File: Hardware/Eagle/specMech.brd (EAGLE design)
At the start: 142.2 x 121.9 mm, 86 parts, among them J1 PINHD-1X8-MOLEX-SHROUD, J2 JST-2-PIN-2B-PH-K-S(LF)(SN), J3 PINHD-1X8-MOLEX-SHROUD, J4 PINHD-1X8-MOLEX-SHROUD, J6 Molex 0022232081, J7 Lantronix XPORT, J8 Molex 0022232081, U1 MCP23008-E/SO, U10 ADS1115, U11 MCP23008-E/SO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

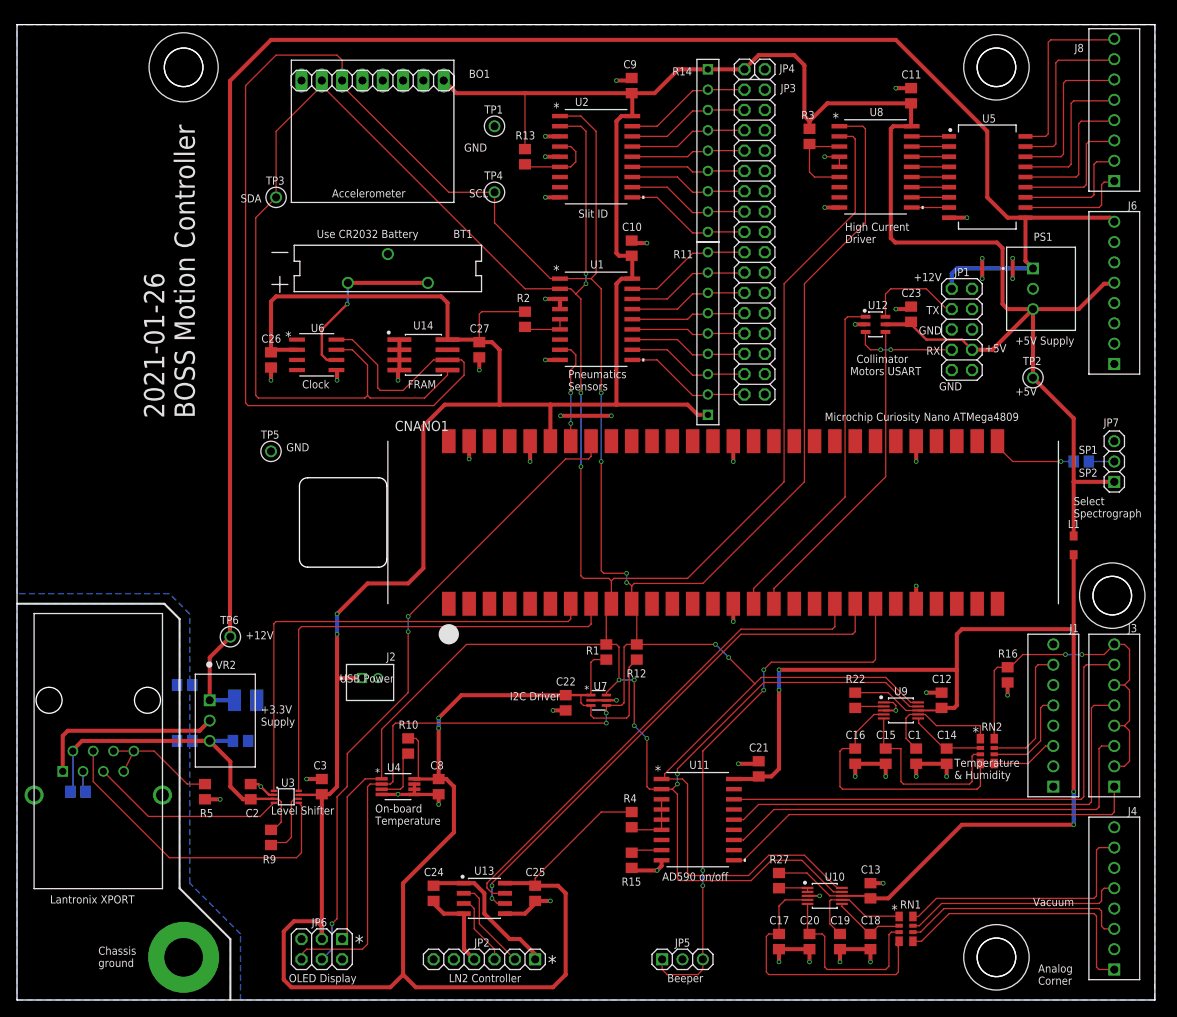
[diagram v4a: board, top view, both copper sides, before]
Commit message: Molex 1x2 header replaces JST header
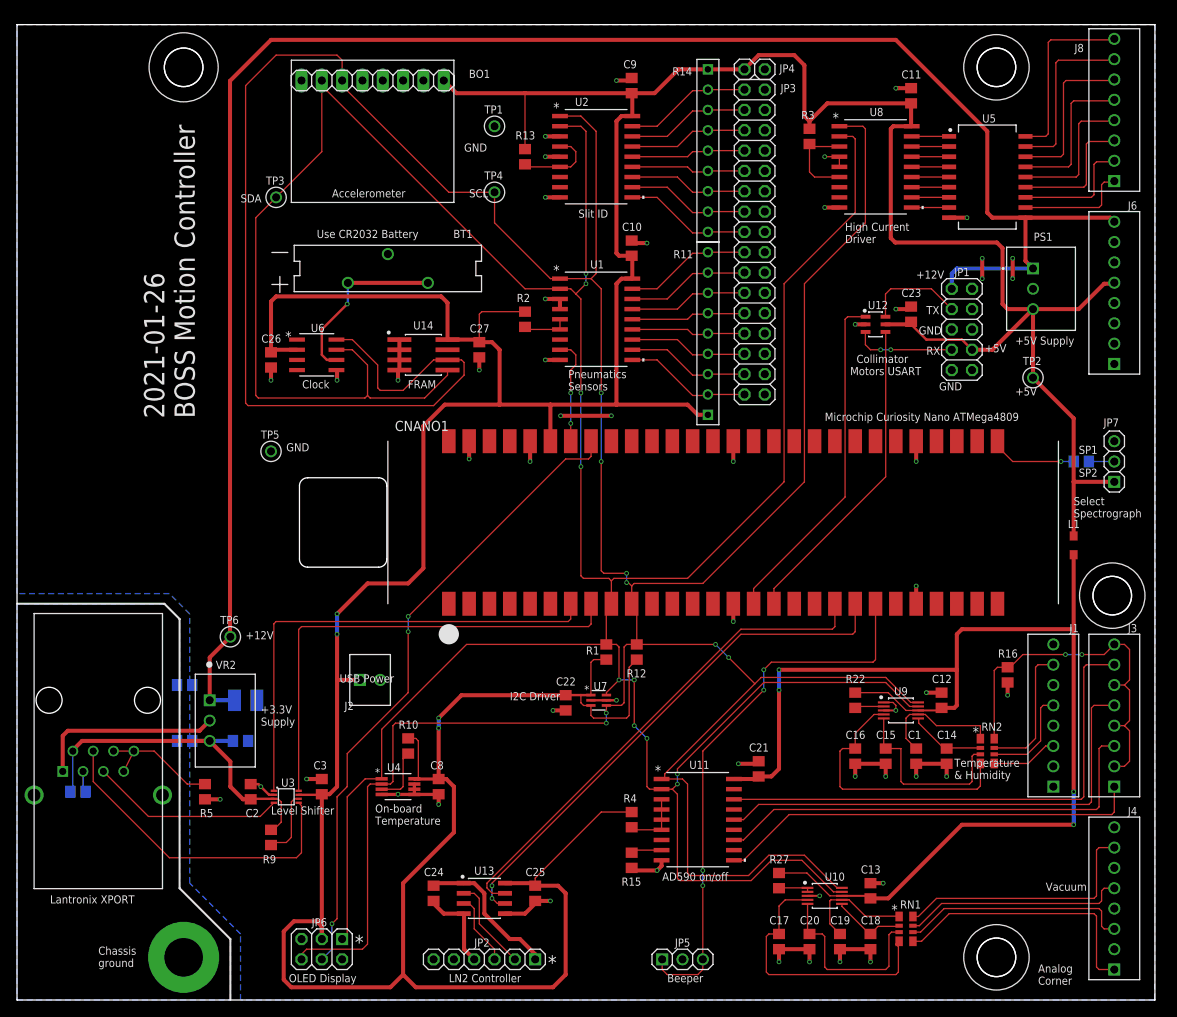
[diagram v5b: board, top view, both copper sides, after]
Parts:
- J2: value JST-2-PIN-2B-PH-K-S(LF)(SN) -> MOLEX-22112022; device AUmlib:JST_B2B-PH-K-S(LF)(SN) -> AUmlib:1X02-MOLEX-22112022
- moved J2 0.32 mm to (44.1, 40.0), turned to 0 degrees
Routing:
- net +12V: track 227.6 -> 228.7 mm
- net SDA: track 430.4 -> 431.0 mm
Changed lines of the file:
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@@
 <wire x1="142.24" y1="121.92" x2="0" y2="121.92" width="0" layer="20"/>
 <text x="40.3225" y="39.6875" size="1.016" layer="25" font="vector">USB Power</text>
-<text x="112.0775" y="89.8525" size="1.016" layer="25" font="vector">+12V</text>
+<text x="112.395" y="90.17" size="1.016" layer="25" font="vector">+12V</text>
 <text x="120.9675" y="80.9625" size="1.016" layer="25" font="vector">+5V</text>
 <text x="115.2525" y="76.2" size="1.016" layer="25" font="vector">GND</text>
@@
 <text x="31.75" y="23.1775" size="1.016" layer="25" font="vector">Level Shifter</text>
 <text x="4.1275" y="12.065" size="1.016" layer="25" font="vector">Lantronix XPORT</text>
-<text x="127" y="11.7475" size="1.016" layer="25" font="vector">Vacuum</text>
+<text x="128.5875" y="13.6525" size="1.016" layer="25" font="vector">Vacuum</text>
 <text x="117.1575" y="27.6225" size="1.016" layer="25" font="vector">Temperature
 &amp; Humidity</text>
@@
 <attribute name="NAME" x="117.1575" y="90.4875" size="1.016" layer="25" font="vector"/>
 <attribute name="POPULARITY" value="35" x="127" y="83.82" size="1.778" layer="27" rot="R270" display="off"/>
-<attribute name="VALUE" x="113.665" y="90.17" size="1.016" layer="27" font="vector" rot="R270"/>
 </element>
 <element name="U12" library="AUmlib" library_urn="urn:adsk.eagle:library:9166017" package="SOP95P275X110-6" package3d_urn="urn:adsk.eagle:package:9152015/2" value="74HC2G17TSSOP-6" x="107.315" y="84.455" smashed="yes">
@@
 <element name="JP2" library="AUmlib" library_urn="urn:adsk.eagle:library:9166017" package="1X06" package3d_urn="urn:adsk.eagle:package:24493396/1" value="1x6 pinhdr" x="58.42" y="5.08" smashed="yes" rot="R180">
 <attribute name="NAME" x="57.15" y="6.6675" size="1.016" layer="25" font="vector"/>
-<attribute name="VALUE" x="66.04" y="8.255" size="1.27" layer="27" rot="R180"/>
 </element>
 <element name="C24" library="AUmlib" library_urn="urn:adsk.eagle:library:9166017" package="C0805" package3d_urn="urn:adsk.eagle:package:4021265/3" value="0.1uF" x="52.07" y="13.335" smashed="yes" rot="R270">
@@
 </element>
 <element name="J7" library="AUmlib" library_urn="urn:adsk.eagle:library:9166017" package="XPORT-2" package3d_urn="urn:adsk.eagle:package:18328251/5" value="Lantronix XPORT" x="10.16" y="31.115" smashed="yes" rot="R270"/>
-<element name="J2" library="AUmlib" library_urn="urn:adsk.eagle:library:9166017" package="JST_B2B-PH-K-S(LF)(SN)" package3d_urn="urn:adsk.eagle:package:24616272/2" value="JST-2-PIN-2B-PH-K-S(LF)(SN)" x="44.1325" y="39.6875" smashed="yes" rot="R180">
-<attribute name="DESCRIPTION" value=" Connector Header Through Hole 2 position 0.079 (2.00mm) " x="44.1325" y="39.6875" size="1.778" layer="27" rot="R180" display="off"/>
-<attribute name="DIGI-KEY_PART_NUMBER" value="455-1704-ND" x="44.1325" y="39.6875" size="1.778" layer="27" rot="R180" display="off"/>
-<attribute name="MF" value="JST Sales" x="44.1325" y="39.6875" size="1.778" layer="27" rot="R180" display="off"/>
-<attribute name="MP" value="B2B-PH-K-S(LF)(SN)" x="44.1325" y="39.6875" size="1.778" layer="27" rot="R180" display="off"/>
-<attribute name="NAME" x="47.33731875" y="43.43358125" size="1.016" layer="25" font="vector" rot="R180"/>
-<attribute name="PACKAGE" value="None" x="44.1325" y="39.6875" size="1.778" layer="27" rot="R180" display="off"/>
-<attribute name="PURCHASE-URL" value="https://pricing.snapeda.com/search/part/B2B-PH-K-S(LF)(SN)/?ref=eda" x="44.1325" y="39.6875" size="1.778" layer="27" rot="R180" display="off"/>
+<element name="J2" library="AUmlib" library_urn="urn:adsk.eagle:library:9166017" package="1X02-MOLEX-22112022" package3d_urn="urn:adsk.eagle:package:24727026/5" value="MOLEX-22112022" x="44.1325" y="40.005" smashed="yes">
+<attribute name="NAME" x="40.92768125" y="36.25891875" size="1.016" layer="25" font="vector"/>
 </element>
 <element name="JP7" library="AUmlib" library_urn="urn:adsk.eagle:library:9166017" package="1X03" package3d_urn="urn:adsk.eagle:package:21589412/1" value="1x3 pinhdr" x="137.16" y="67.31" smashed="yes" rot="R90">
@@
 <wire x1="71.7375" y1="35.5775" x2="71.7375" y2="36.815" width="0.1524" layer="1"/>
 <wire x1="72.0725" y1="35.2425" x2="71.7375" y2="35.5775" width="0.1524" layer="1"/>
-<wire x1="43.1325" y1="40.2375" x2="40.2375" y2="40.2375" width="0.508" layer="1"/>
-<wire x1="40.2375" y1="40.2375" x2="40.005" y2="40.005" width="0.508" layer="1"/>
 <wire x1="64.77" y1="14.285" x2="64.77" y2="15.24" width="0.1524" layer="1"/>
 <wire x1="64.77" y1="15.24" x2="73.025" y2="23.495" width="0.1524" layer="1"/>
@@
 <wire x1="53.8135" y1="87.1565" x2="53.0225" y2="87.9475" width="0.508" layer="1"/>
 <wire x1="53.0225" y1="87.9475" x2="32.385" y2="87.9475" width="0.508" layer="1"/>
+<wire x1="42.8625" y1="40.005" x2="40.005" y2="40.005" width="0.508" layer="1"/>
 </signal>
 <signal name="XP-TX">
@@
 <wire x1="24.085" y1="42.8175" x2="26.67" y2="45.4025" width="0.508" layer="1"/>
 <wire x1="26.625" y1="45.4475" x2="26.67" y2="45.4025" width="0.508" layer="1"/>
-<wire x1="126.0576" y1="97.79" x2="123.825" y2="97.79" width="0.508" layer="1"/>
-<wire x1="123.825" y1="97.79" x2="121.285" y2="100.33" width="0.508" layer="1"/>
-<wire x1="121.285" y1="100.33" x2="121.285" y2="108.585" width="0.508" layer="1"/>
+<wire x1="126.0576" y1="97.79" x2="121.92" y2="97.79" width="0.508" layer="1"/>
+<wire x1="121.92" y1="97.79" x2="121.285" y2="98.425" width="0.508" layer="1"/>
+<wire x1="121.285" y1="98.425" x2="121.285" y2="108.585" width="0.508" layer="1"/>
 <wire x1="121.285" y1="108.585" x2="109.855" y2="120.015" width="0.508" layer="1"/>
 <wire x1="109.855" y1="120.015" x2="31.75" y2="120.015" width="0.508" layer="1"/>
@@
 <wire x1="95.885" y1="64.77" x2="83.82" y2="52.705" width="0.1524" layer="1"/>
 <wire x1="38.1" y1="114.935" x2="38.1" y2="114.3" width="0.1524" layer="1"/>
-<wire x1="38.1" y1="114.3" x2="32.385" y2="108.585" width="0.1524" layer="1"/>
 <wire x1="30.1625" y1="75.2475" x2="29.845" y2="75.565" width="0.1524" layer="1"/>
 <wire x1="67.8688" y1="88.9" x2="69.215" y2="88.9" width="0.1524" layer="1"/>
@@
 <wire x1="29.845" y1="75.565" x2="29.845" y2="97.79" width="0.1524" layer="1"/>
 <wire x1="29.845" y1="97.79" x2="32.385" y2="100.33" width="0.1524" layer="1"/>
-<wire x1="32.385" y1="108.585" x2="32.385" y2="100.33" width="0.1524" layer="1"/>
 <wire x1="63.5" y1="88.9" x2="38.1" y2="114.3" width="0.1524" layer="1"/>
 <wire x1="67.8688" y1="88.9" x2="63.5" y2="88.9" width="0.1524" layer="1"/>
@@
 <wire x1="43.4975" y1="75.2475" x2="43.815" y2="75.565" width="0.1524" layer="1"/>
 <wire x1="30.1625" y1="75.2475" x2="43.4975" y2="75.2475" width="0.1524" layer="1"/>
+<wire x1="38.1" y1="114.935" x2="38.1" y2="106.045" width="0.1524" layer="1"/>
+<wire x1="38.1" y1="106.045" x2="32.385" y2="100.33" width="0.1524" layer="1"/>
 </signal>
 <signal name="N$1">
@@
 <contactref element="JP1" pad="3"/>
 <wire x1="108.5592" y1="85.405" x2="108.5592" y2="88.2392" width="0.1524" layer="1"/>
-<wire x1="109.22" y1="88.9" x2="113.665" y2="88.9" width="0.1524" layer="1"/>
-<wire x1="113.665" y1="88.9" x2="116.205" y2="86.36" width="0.1524" layer="1"/>
-<wire x1="116.205" y1="86.36" x2="116.84" y2="86.36" width="0.1524" layer="1"/>
+<wire x1="109.22" y1="88.9" x2="114.3" y2="88.9" width="0.1524" layer="1"/>
+<wire x1="114.3" y1="88.9" x2="116.84" y2="86.36" width="0.1524" layer="1"/>
 <wire x1="108.5592" y1="88.2392" x2="109.22" y2="88.9" width="0.1524" layer="1"/>
 </signal>

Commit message: Added TVS diodes on ADC inputs
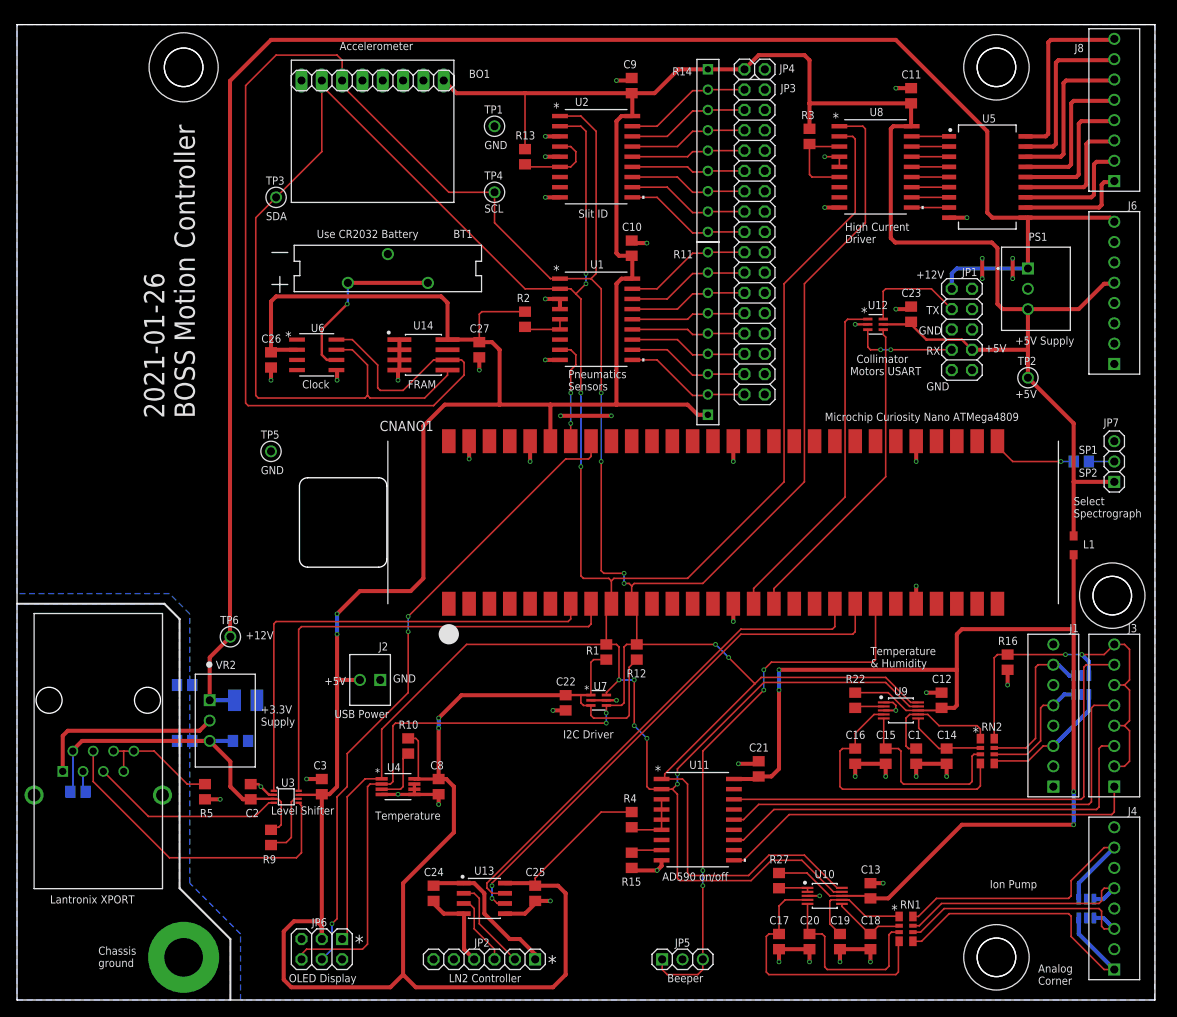
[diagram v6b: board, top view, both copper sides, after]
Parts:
- added TVS1, TVS2: TVS-QUAD-ESDA6V1BC6, AUmlib:SOT95P280X145-6N
- U12: value 74HC2G17TSSOP-6 -> SCHMITT-TRIG-NC7WZ17P6X; device AUmlib:SOP95P275X110-6 -> AUmlib:SC70-6_ONS
- moved R16 1.59 mm to (123.8, 42.2)
- moved PS1 0.64 mm to (126.4, 88.9)
- moved TP2 0.64 mm to (126.4, 77.8)
- turned J2 to 180 degrees
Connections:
- net LN-RX renamed NANO-TX3
- net LN-TX renamed NANO-RX3
- net N$19 renamed COLL-RX
- net N$8 renamed COLL-TX
- net RC-RX renamed NANO-TX2
- net RC-TX renamed NANO-RX2
- net RX renamed NANO-RX1
- net TX renamed NANO-TX1
- net +5V: now also J2.2; no longer J2.1
- net A0A: now also TVS2.4
- net A0B: now also TVS1.6
- net A1A: now also TVS2.6
- net A1B: now also TVS1.4
- net A2A: now also TVS2.1
- net A2B: now also TVS1.3
- net A3A: now also TVS2.3
- net A3B: now also TVS1.1
- net GND: now also J2.1, TVS1.2, TVS1.5, TVS2.2, TVS2.5; no longer J2.2
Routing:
- net A0A: track 8.33 -> 16.6 mm
- net A3B: track 32.1 -> 38.1 mm
- net A0B: track 33.2 -> 39.3 mm
- net A3A: track 46.8 -> 50.7 mm
- net A2A: track 16.9 -> 20.0 mm
- net A1A: track 12.3 -> 15.5 mm
- net A2B: track 27.9 -> 31.0 mm
- net A1B: track 28.6 -> 31.7 mm
- net +5V: track 589.1 -> 587.5 mm
- net +12V: track 228.7 -> 227.7 mm
- net COLL-RX: track 12.4 -> 13.2 mm
- net SDA: track 431.0 -> 430.4 mm
- net GND: track 160.0 -> 160.6 mm
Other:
- board text added: "Ion Pump"
- board text added: "Temperature"
- board text removed: "On-board Temperature"
- board text removed: "Vacuum"

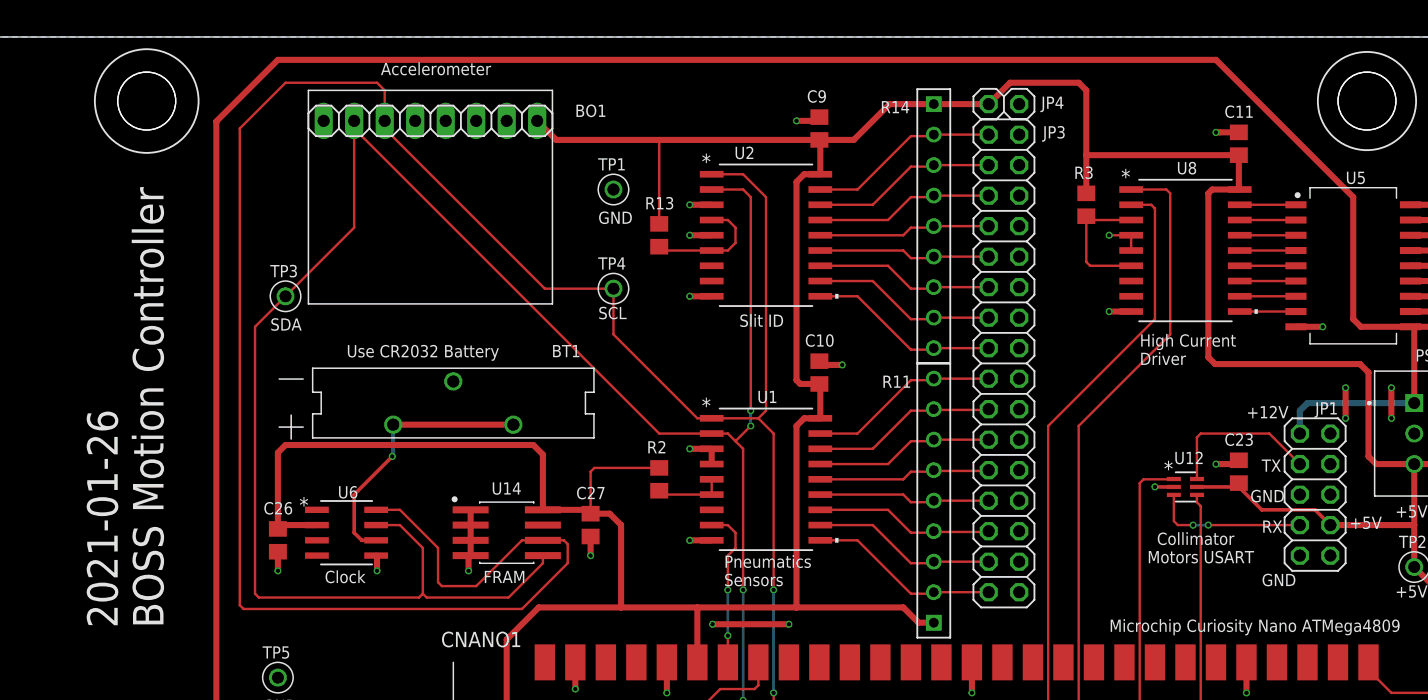
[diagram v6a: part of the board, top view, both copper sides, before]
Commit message: Moved the accelerometer a bit away from board edge
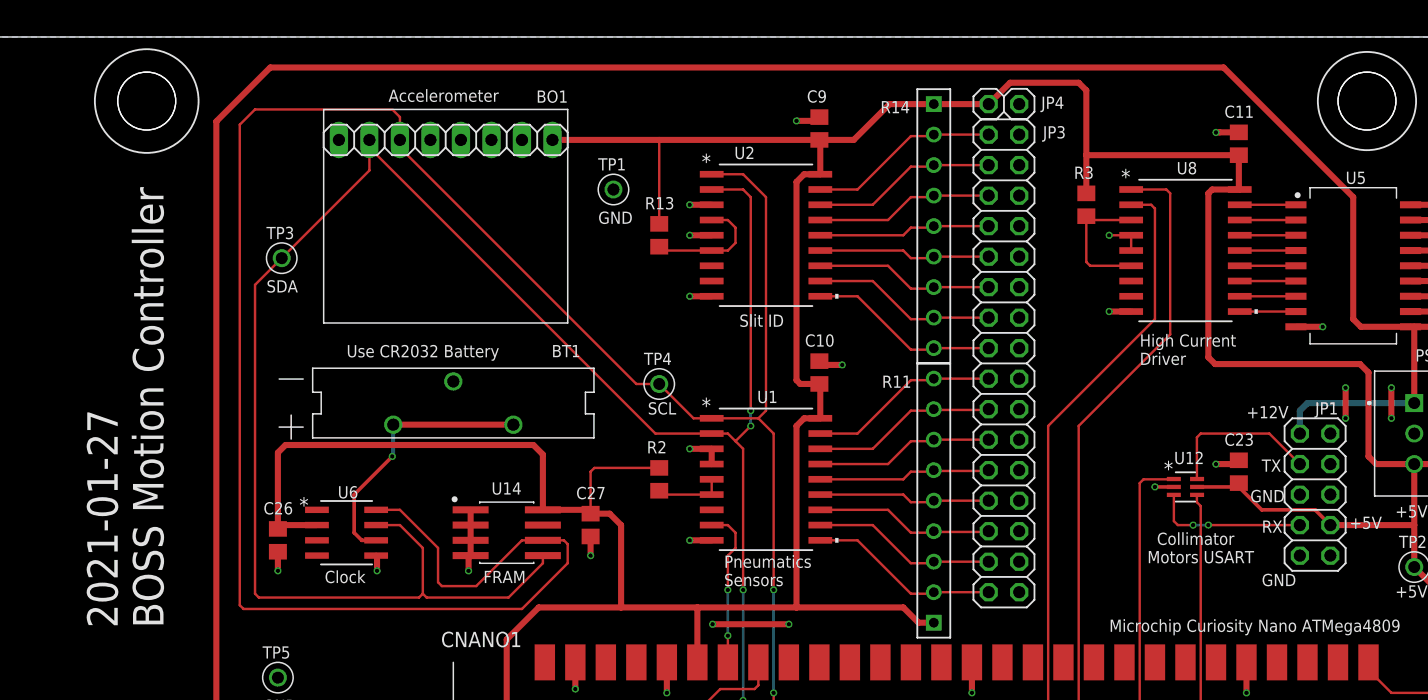
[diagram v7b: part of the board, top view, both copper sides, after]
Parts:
- moved TP4 8.80 mm to (63.5, 93.0)
- moved TP3 3.19 mm to (32.1, 103.5)
- moved BO1 2.03 mm to (45.7, 107.0)
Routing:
- net SCL: track 476.1 -> 471.8 mm
- net SDA: track 430.4 -> 428.1 mm
- net +5V: track 587.5 -> 585.6 mm
- net +12V: track 227.7 -> 227.1 mm
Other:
- board text added: "2021-01-27 BOSS Motion Controller"
- board text removed: "2021-01-26 BOSS Motion Controller"

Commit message: Updated part number for high current driver
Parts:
- U5: value TBD62083 -> TBD62083AFWG,EL
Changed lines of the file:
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@@
 <attribute name="VENDOR" value="Bourns Electronics" x="86.36" y="116.332" size="1.778" layer="27" rot="R270" display="off"/>
 </element>
-<element name="U5" library="AUmlib" library_urn="urn:adsk.eagle:library:9166017" package="SOIC127P1030X245-18" package3d_urn="urn:adsk.eagle:package:10465865/2" value="TBD62083" x="121.285" y="102.87" smashed="yes">
+<element name="U5" library="AUmlib" library_urn="urn:adsk.eagle:library:9166017" package="SOIC127P1030X245-18" package3d_urn="urn:adsk.eagle:package:10465865/2" value="TBD62083AFWG,EL" x="121.285" y="102.87" smashed="yes">
 <attribute name="NAME" x="120.65" y="109.6875" size="1.016" layer="25" font="vector"/>
 </element>
